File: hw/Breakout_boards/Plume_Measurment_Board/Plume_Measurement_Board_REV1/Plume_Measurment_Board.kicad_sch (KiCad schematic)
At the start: 18 parts, among them U1 AD7124-8BCPZ-RL, U2 LMP7721MA/NOPB, U3 LMP2022MA/NOPB, U4 AD8475ARMZ, U5 AD8475ARMZ

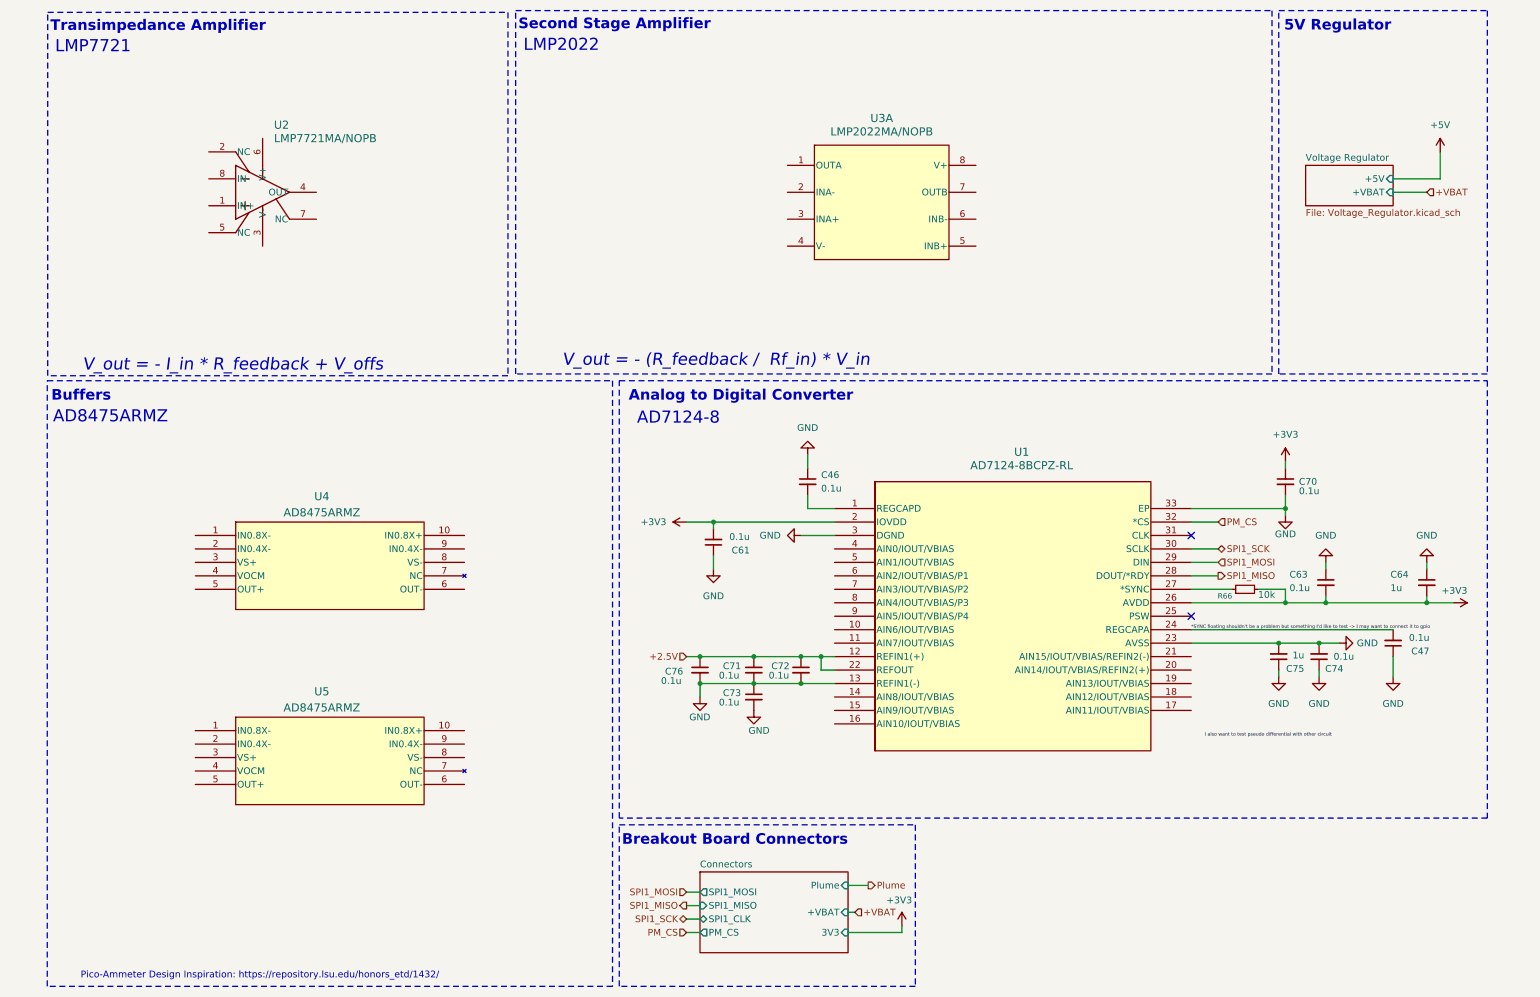
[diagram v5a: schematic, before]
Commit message: New AD7124 Chip
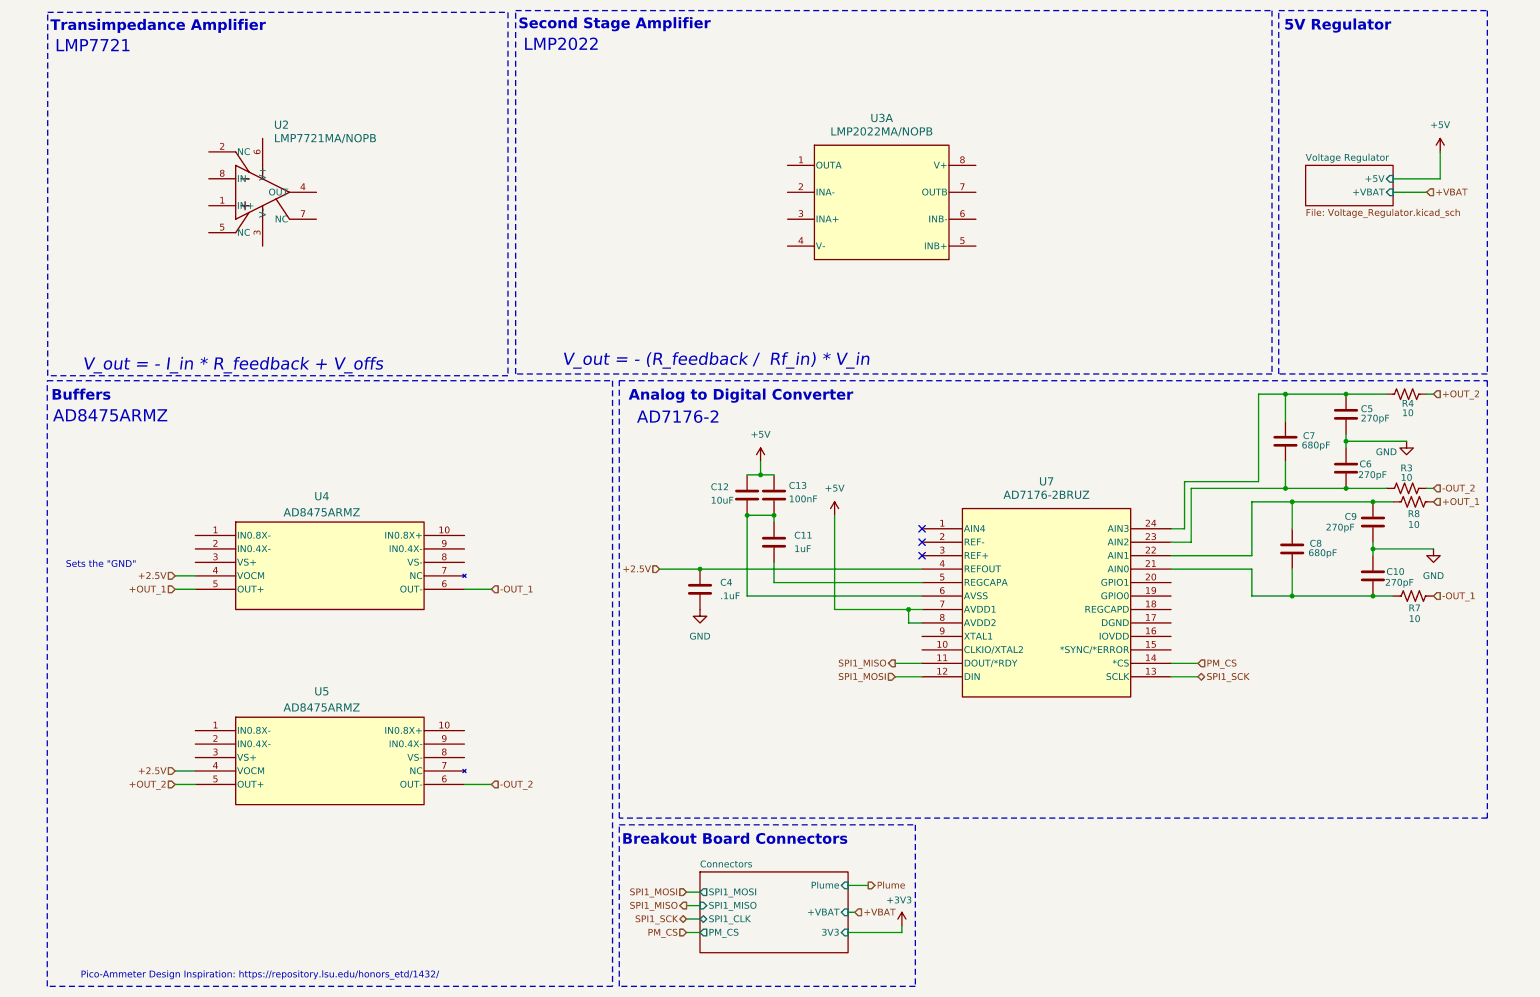
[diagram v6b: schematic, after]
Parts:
- removed C46, C47, C61, C63, C70, C71, C72, C73, C74, C76: 0.1u, Capacitor_SMD:C_0603_1608Metric, symbol Device:C_Small
- removed C64, C75: 1u, Capacitor_SMD:C_0603_1608Metric, symbol Device:C_Small
- removed R66: 10k, Resistor_SMD:R_0603_1608Metric, symbol Device:R_Small
- removed U1: AD7124-8BCPZ-RL, CP-32-12_ADI, symbol ADC_Analog_Devices:AD7124-8BCPZ-RL
- added C10, C5, C6, C9: 270pF, Capacitor_SMD:C_0603_1608Metric_Pad1.08x0.95mm_HandSolder, symbol Device:C
- added C11: 1uF, Capacitor_SMD:C_0603_1608Metric_Pad1.08x0.95mm_HandSolder, symbol Device:C
- added C12: 10uF, Capacitor_SMD:C_0805_2012Metric_Pad1.18x1.45mm_HandSolder, symbol Device:C
- added C13: 100nF, Capacitor_SMD:C_0603_1608Metric_Pad1.08x0.95mm_HandSolder, symbol Device:C
- added C4: .1uF, Capacitor_SMD:C_0603_1608Metric_Pad1.08x0.95mm_HandSolder, symbol Device:C
- added C7, C8: 680pF, Capacitor_SMD:C_0603_1608Metric_Pad1.08x0.95mm_HandSolder, symbol Device:C
- added R3, R4, R7, R8: 10, Resistor_SMD:R_0603_1608Metric_Pad0.98x0.95mm_HandSolder, symbol Device:R_US
- added U7: AD7176-2BRUZ, ADC_Analog_Devices:RU_24_ADI, symbol ADC_Analog_Devices:AD7176-2BRUZ
- U2, U3: footprint M08A -> Amplifier_Texas_Instruments:M08A
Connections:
- net +2.5V: now also U4.4 (VOCM), U5.4 (VOCM), C4.1, U7.4 (REFOUT)
- net +5V: now also C12.2, C13.2, U7.7 (AVDD1), U7.8 (AVDD2)
- net GND: now also C10.1, C4.2, C5.2, C6.1, C9.2
- net PM_CS: now also U7.14 (*CS)
- net SPI1_MISO: now also U7.11 (DOUT/*RDY)
- net SPI1_MOSI: now also U7.12 (DIN)
- net SPI1_SCK: now also U7.13 (SCLK)
- net +OUT_1: now reaches U4.5 (OUT+)
- net +OUT_1: now also R8.2
- net -OUT_1: now reaches U4.6 (OUT-)
- net -OUT_1: now also R7.2
- net +OUT_2: now reaches U5.5 (OUT+)
- net +OUT_2: now also R4.2
- net -OUT_2: now reaches U5.6 (OUT-)
- net -OUT_2: now also R3.2
- new net: C8.1, C9.1, R8.1, U7.22 (AIN1)
- new net: C10.2, C8.2, R7.1, U7.21 (AIN0)
- new net: C5.1, C7.1, R4.1, U7.24 (AIN3)
- new net: C6.2, C7.2, R3.1, U7.23 (AIN2)
- new net: C11.1, U7.5 (REGCAPA)
- new net: C11.2, C12.1, C13.1, U7.6 (AVSS)
- no-connect marks 2 -> 3
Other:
- note added: "AD7176-2"
- note added: "Sets the "GND""
- note removed: "AD7124-8"

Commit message: Routing Process w/ AD7176
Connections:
- net GND: no longer C4.2
- net VSS: now reaches C11.2, C12.1, C13.1, U7.6 (AVSS)
- net VSS: now also C4.2
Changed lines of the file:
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@@
 	(wire
 		(pts
-			(xy 161.29 107.95) (xy 161.29 125.73)
+			(xy 161.29 115.57) (xy 161.29 125.73)
 		)
 		(stroke
@@
 	(wire
 		(pts
+			(xy 134.62 107.95) (xy 144.78 107.95)
+		)
+		(stroke
+			(width 0)
+			(type default)
+		)
+	)
+	(wire
+		(pts
+			(xy 134.62 129.54) (xy 135.89 129.54)
+		)
+		(stroke
+			(width 0)
+			(type default)
+		)
+	)
+	(wire
+		(pts
 			(xy 177.8 128.27) (xy 175.26 128.27)
 		)
@@
 	(wire
 		(pts
+			(xy 135.89 129.54) (xy 135.89 125.73)
+		)
+		(stroke
+			(width 0)
+			(type default)
+		)
+	)
+	(wire
+		(pts
 			(xy 262.89 105.41) (xy 266.7 105.41)
 		)
@@
 		(shape input)
 		(at 133.35 186.69 180)
+		(effects
+			(font
+				(size 1.27 1.27)
+			)
+			(justify right)
+		)
+	)
+	(hierarchical_label "VSS"
+		(shape input)
+		(at 134.62 107.95 180)
 		(effects
 			(font
@@
 		(shape input)
 		(at 36.83 156.21 180)
+		(effects
+			(font
+				(size 1.27 1.27)
+			)
+			(justify right)
+		)
+	)
+	(hierarchical_label "VSS"
+		(shape input)
+		(at 134.62 129.54 180)
 		(effects
 			(font
@@
 	(symbol
 		(lib_id "power:+3V3")
-		(at 161.29 107.95 0)
+		(at 161.29 115.57 0)
 		(unit 1)
 		(body_style 1)
@@
 		(fields_autoplaced yes)
 		(property "Reference" "#PWR0248"
-			(at 161.29 111.76 0)
+			(at 161.29 119.38 0)
 			(hide yes)
 			(show_name no)
@@
 		)
 		(property "Value" "+5V"
-			(at 161.29 102.87 0)
+			(at 161.29 110.49 0)
 			(show_name no)
 			(do_not_autoplace no)
@@
 		)
 		(property "Footprint" ""
-			(at 161.29 107.95 0)
+			(at 161.29 115.57 0)
 			(hide yes)
 			(show_name no)
@@
 		)
 		(property "Datasheet" ""
-			(at 161.29 107.95 0)
+			(at 161.29 115.57 0)
 			(hide yes)
 			(show_name no)
@@
 		)
 		(property "Description" "Power symbol creates a global label with name \"+3V3\""
-			(at 161.29 107.95 0)
+			(at 161.29 115.57 0)
 			(hide yes)
 			(show_name no)
@@
 					(unit 1)
 				)
-			)
-		)
-	)
-	(symbol
-		(lib_id "power:GND")
-		(at 135.89 125.73 0)
-		(unit 1)
-		(body_style 1)
-		(exclude_from_sim no)
-		(in_bom yes)
-		(on_board yes)
-		(in_pos_files yes)
-		(dnp no)
-		(fields_autoplaced yes)
-		(property "Reference" "#PWR05"
-			(at 135.89 132.08 0)
-			(hide yes)
-			(show_name no)
-			(do_not_autoplace no)
-			(effects
-				(font
-					(size 1.27 1.27)
-				)
-			)
-		)
-		(property "Value" "GND"
-			(at 135.89 130.81 0)
-			(show_name no)
-			(do_not_autoplace no)
-			(effects
-				(font
-					(size 1.27 1.27)
-				)
-			)
-		)
-		(property "Footprint" ""
-			(at 135.89 125.73 0)
-			(hide yes)
-			(show_name no)
-			(do_not_autoplace no)
-			(effects
-				(font
-					(size 1.27 1.27)
-				)
-			)
-		)
-		(property "Datasheet" ""
-			(at 135.89 125.73 0)
-			(hide yes)
-			(show_name no)
-			(do_not_autoplace no)
-			(effects
-				(font
-					(size 1.27 1.27)
-				)
-			)
-		)
-		(property "Description" "Power symbol creates a global label with name \"GND\" , ground"
-			(at 135.89 125.73 0)
-			(hide yes)
-			(show_name no)
-			(do_not_autoplace no)
-			(effects
-				(font
-					(size 1.27 1.27)
-				)
-			)
-		)
-		(pin "1"
-		)
-		(instances
-			(project "Plume_Measurment_Board"
-				(path "/2e1d3673-27b9-4604-80fb-036cec98a912"
-					(reference "#PWR05")
-					(unit 1)
-				)

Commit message: AD8475 Buffer Footprint Addition
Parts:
- U4, U5: footprint RM_10_ADI -> Buffer_Analog_Devices:RM_10_ADI
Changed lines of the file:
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@@
 			)
 		)
-		(property "Footprint" "RM_10_ADI"
+		(property "Footprint" "Buffer_Analog_Devices:RM_10_ADI"
 			(at 20.32 111.76 0)
 			(hide yes)
@@
 			)
 		)
-		(property "Footprint" "RM_10_ADI"
+		(property "Footprint" "Buffer_Analog_Devices:RM_10_ADI"
 			(at 20.32 148.59 0)
 			(hide yes)
